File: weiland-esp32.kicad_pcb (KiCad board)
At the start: 2 copper layers, 58.5 x 24.2 mm, 38 parts, among them J1 S02B-PASK-2, J6 S02B-PASK-2, J7 S02B-PASK-2, P1 S04B-PASK-2_LF__SN_, P2 S04B-PASK-2_LF__SN_, U1 ESP32-WROOM-32E(8MB), U2 AMS1117-3.3_C347222, U3 MAX98357AETE_T, U5 ULN2003F12FN-7, U6 DZ127S-22-06-55

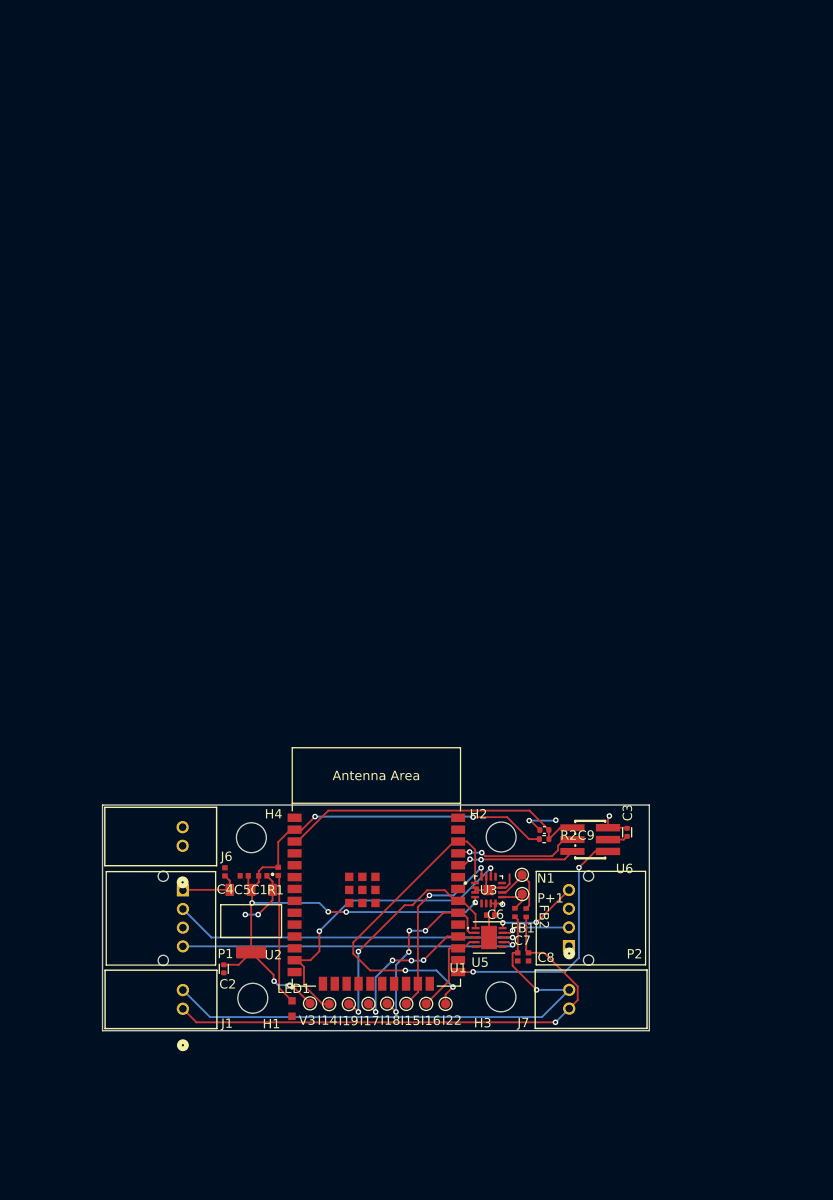
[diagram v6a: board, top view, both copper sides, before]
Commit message: working board but wrong placement of holes
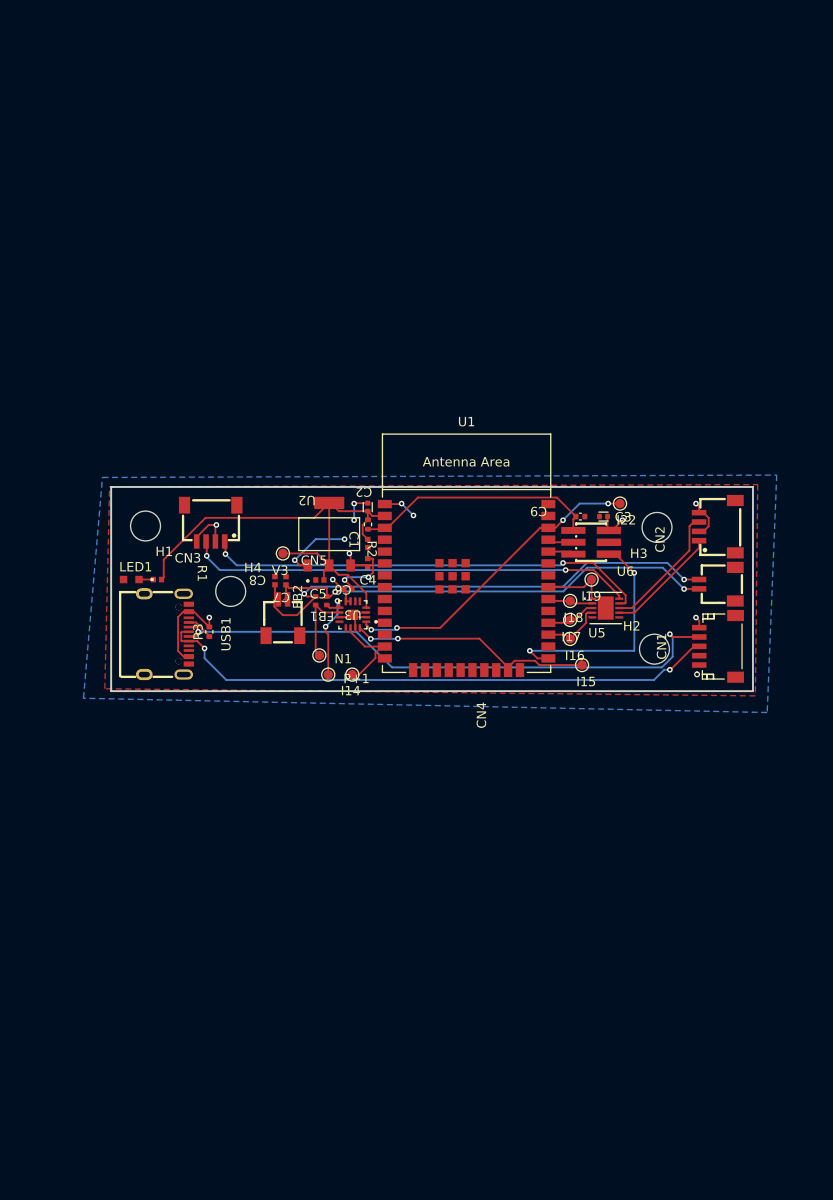
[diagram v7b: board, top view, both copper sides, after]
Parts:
- removed J1, J6, J7: S02B-PASK-2, footprints:CONN2_S02B-PASK-2_JST
- removed P1, P2: S04B-PASK-2_LF__SN_, S04B-PASK-2_LF__SN_:JST_S04B-PASK-2
- added CN1: SM05B-SRSS-TB (LF)(SN), easyeda2kicad:CONN-SMD_SM05B-SRSS-TB-LF-SN, F.Cu at (195.6, 70.9)
- added CN2: SM04B-SRSS-TB (LF)(SN), easyeda2kicad:CONN-SMD_4P-P1.00_SM04B-SRSS-TB-LF-SN, F.Cu at (195.6, 58.1)
- added CN3: SM04B-SRSS-TB (LF)(SN), easyeda2kicad:CONN-SMD_4P-P1.00_SM04B-SRSS-TB-LF-SN, F.Cu at (141.4, 57.7)
- added CN4: SM02B-SRSS-TB (LF)(SN), easyeda2kicad:CONN-SMD_2P-P1.00_SM02B-SRSS-TB-LF-SN, F.Cu at (195.6, 64.2)
- added CN5: SM02B-SRSS-TB (LF)(SN), easyeda2kicad:CONN-SMD_2P-P1.00_SM02B-SRSS-TB-LF-SN, F.Cu at (149.1, 67.8)
- added R3: 56kOhm, Resistor_SMD:R_0402_1005Metric, F.Cu at (141.2, 69.3)
- added USB1: TYPE-C 16PIN 2MD(073), easyeda2kicad:USB-C-SMD_TYPE-C-6PIN-2MD-073, F.Cu at (136.7, 69.6)
- moved I22 56.7 mm to (185.2, 55.6)
- moved H3 52.9 mm to (189.1, 58.2)
- moved I19 52.3 mm to (182.1, 63.8)
- moved H1 51.8 mm to (134.4, 58.0)
- moved C2 51.7 mm to (158.2, 56.0), turned to -90 degrees
- moved LED1 49.0 mm to (132.9, 63.8), turned to 180 degrees
- moved C8 48.5 mm to (148.2, 63.9), turned to 90 degrees
- moved V3 48.2 mm to (149.1, 61.0)
- moved I18 47.3 mm to (179.8, 66.0)
- moved C7 47.3 mm to (149.4, 63.9), turned to 90 degrees
- moved I17 46.4 mm to (179.8, 68.1)
- moved U2 42.2 mm to (154.1, 58.9), turned to 90 degrees
- moved I16 42.0 mm to (179.8, 70.1)
- moved I15 40.8 mm to (181.1, 72.9)
- moved FB2 40.3 mm to (152.6, 66.0), turned to 90 degrees
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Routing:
- net /Dn: track 0.00 -> 61.4 mm, vias 0 -> 2
- net /Dp: track 0.00 -> 61.0 mm, vias 0 -> 2
- net /OUTB: track 7.35 -> 47.9 mm, vias 1 -> 2
- net /OUTA: track 9.09 -> 47.9 mm
- net +3.3V: track 83.5 -> 53.2 mm, vias 8 -> 0
- net /OUTD: track 36.5 -> 12.2 mm, vias 1 -> 0
- net /IO14: track 34.1 -> 9.76 mm, vias 2 -> 0
- net /OUTC: track 37.6 -> 13.9 mm, vias 1 -> 0
- net /IO19: track 25.7 -> 7.04 mm, vias 2 -> 0
- net +5V: track 12.7 -> 31.2 mm, vias 2 -> 7
- net /IO18: track 20.2 -> 4.89 mm, vias 4 -> 0
- net Net-(LED1-A): track 14.0 -> 1.54 mm
- net /IO17: track 17.5 -> 5.36 mm, vias 4 -> 0
- net /TXD0: track 13.5 -> 2.79 mm, vias 2 -> 0
- net /RXD0: track 12.9 -> 2.79 mm, vias 2 -> 0
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- added copper zone on B.Cu, net +5V
- added copper zone on F.Cu, net GND
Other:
- board size 58.5 x 24.2 mm -> 68.7 x 21.8 mm

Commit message: fully routed board
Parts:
- moved P+1 38.6 mm to (154.7, 35.3)
- moved V3 34.5 mm to (149.4, 26.4)
- moved N1 34.3 mm to (154.7, 37.6)
- moved R3 33.1 mm to (143.0, 36.3)
- moved FB1 32.0 mm to (152.1, 34.0), turned to 180 degrees
- moved LED1 31.4 mm to (135.6, 32.5)
- moved R1 31.4 mm to (138.4, 32.5)
- moved CN3 30.9 mm to (144.0, 26.9)
- moved CN1 30.9 mm to (197.9, 40.1)
- moved CN2 30.9 mm to (197.8, 27.3)
- moved CN4 30.9 mm to (197.8, 33.5)
- moved I22 30.8 mm to (182.6, 24.9)
- moved H3 30.8 mm to (191.3, 27.4)
- moved FB2 30.7 mm to (152.1, 35.3), turned to 180 degrees
- moved H1 30.7 mm to (136.9, 27.4)
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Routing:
- net /OUTP: track 49.2 -> 61.8 mm, vias 2 -> 3
- net GND: track 27.4 -> 21.4 mm, vias 8 -> 6
- net /IO0: track 25.4 -> 19.4 mm
- net /PRE-OUTP: track 10.8 -> 4.89 mm, vias 2 -> 0
- net /OUTB: track 47.9 -> 51.2 mm
- net /PRE-OUTN: track 8.44 -> 5.16 mm
- net /Dp: track 61.0 -> 63.9 mm
- net /OUTA: track 47.9 -> 50.0 mm
- net /IO22: track 33.3 -> 31.3 mm
- net +5V: track 31.2 -> 33.1 mm, vias 7 -> 6
- net +3.3V: track 53.2 -> 51.5 mm
- net /IO14: track 9.76 -> 8.29 mm
- net /Dn: track 61.4 -> 62.7 mm
- net /OUTN: track 53.7 -> 52.5 mm
- net /OUTD: track 12.2 -> 13.3 mm
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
